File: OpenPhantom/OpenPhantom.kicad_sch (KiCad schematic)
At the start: 94 parts, among them J1 Barrel_Jack, J2 Video, J3 Audio, Q1 BC548, Q2 BD136, Q3 BC557, Q4 BC548, SW1 POWER, SW2 RESET, U1 UM6116 VRAM, U10 74HC368, U11 74HC368, U2 UM6116 WRAM, U3 74HC04, U4 UA6547_CPU, U5 4013, U6 UA6548_PPU, U7 74HC139, U8 74LS373, U9 LM7805_TO220, Y1 21.453366 MHz

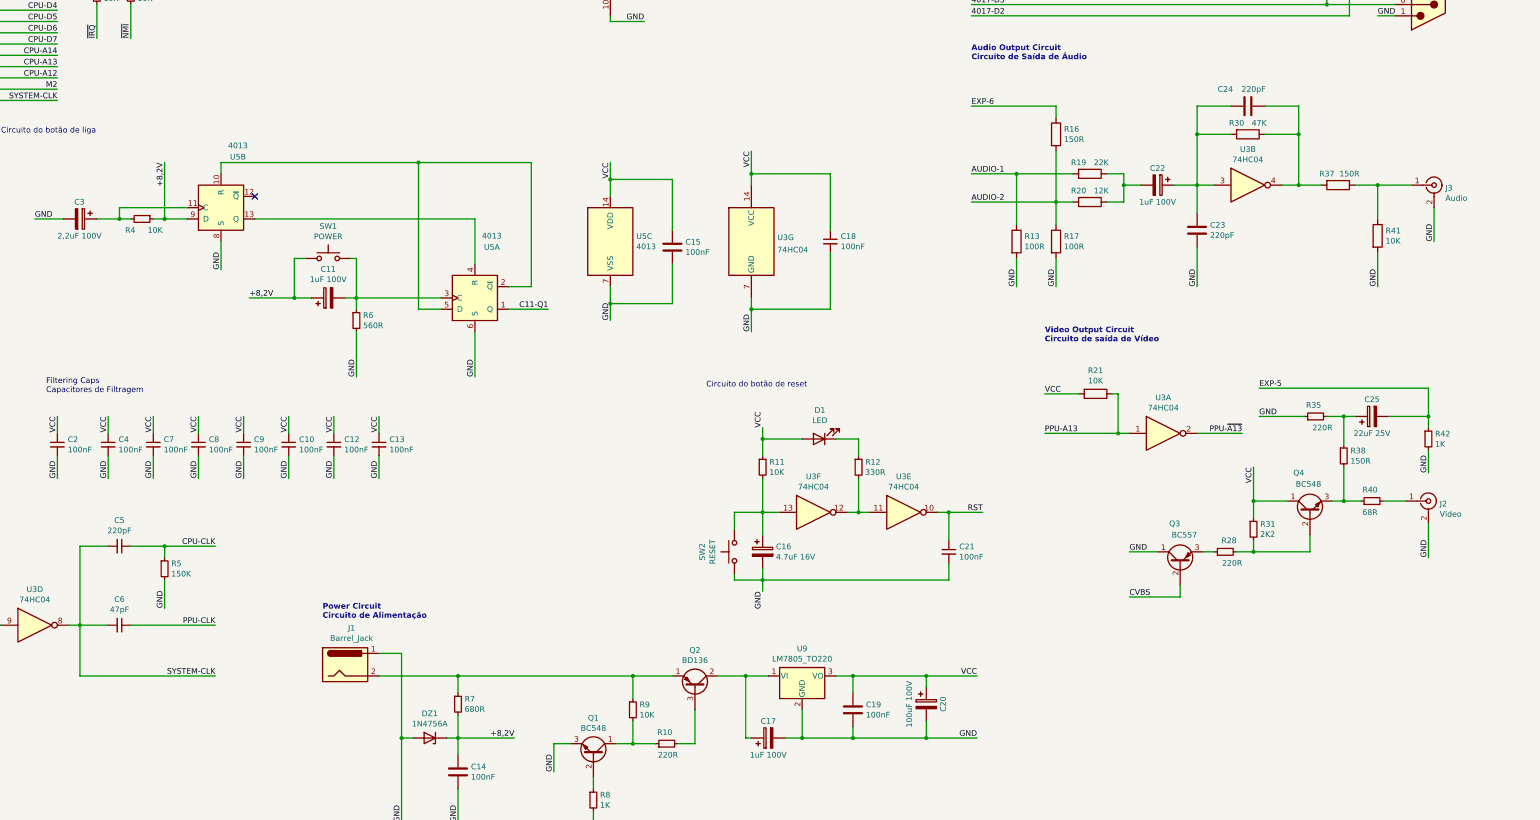
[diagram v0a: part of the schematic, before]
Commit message: PDF + PCB Routing + `Placement
Corrected component position. Added PCB Schematic PDF. Changed the logo. Moved the RCA connectors 2mm closer to the PCB edge.
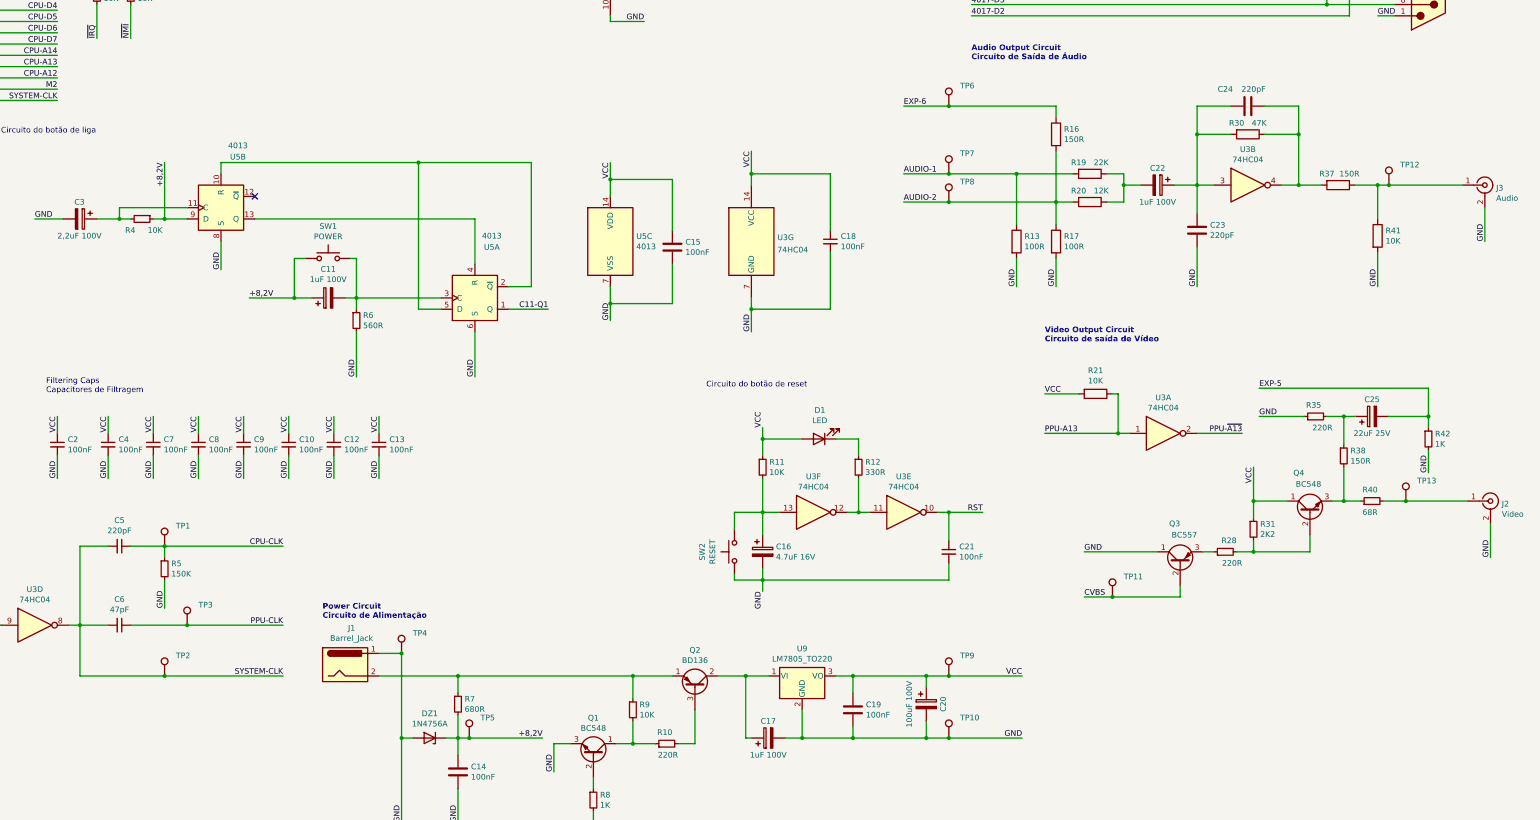
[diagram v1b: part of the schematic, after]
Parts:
- added TP1, TP10, TP11, TP12, TP13, TP2, TP3, TP4, TP5, TP6, TP7, TP8, TP9: (no value), symbol Connector:TestPoint
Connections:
- net +8,2V: now also TP5.1
- net AUDIO-1: now also TP7.1
- net AUDIO-2: now also TP8.1
- net CPU-CLK: now also TP1.1
- net CVBS: now also TP11.1
- net EXP-6: now also TP6.1
- net GND: now also TP10.1, TP4.1
- net PPU-CLK: now also TP3.1
- net SYSTEM-CLK: now also TP2.1
- net VCC: now also TP9.1
- net at J2.1 (In), R40.2: now also TP13.1
- net at J3.1 (In), R37.1, R41.1: now also TP12.1
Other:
- moved on the sheet: J2, J3

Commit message: New BOM + Schematic
Updated Bill of Materials and Schematics
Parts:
- TP1: value (none) -> CPU CLK; footprint (none) -> TestPoint:TestPoint_Pad_1.0x1.0mm
- TP10: value (none) -> GND; footprint (none) -> TestPoint:TestPoint_Pad_1.0x1.0mm
- TP11: value (none) -> PPU CVBS; footprint (none) -> TestPoint:TestPoint_Pad_1.0x1.0mm
- TP12: value (none) -> AUDIO OUT; footprint (none) -> TestPoint:TestPoint_Pad_1.0x1.0mm
- TP13: value (none) -> VIDEO OUT; footprint (none) -> TestPoint:TestPoint_Pad_1.0x1.0mm
- TP2: value (none) -> SYS CLK; footprint (none) -> TestPoint:TestPoint_Pad_1.0x1.0mm
- TP3: value (none) -> PPU CLK; footprint (none) -> TestPoint:TestPoint_Pad_1.0x1.0mm
- TP4: value (none) -> POWER SUPPLY IN; footprint (none) -> TestPoint:TestPoint_Pad_1.0x1.0mm
- TP5: value (none) -> +8,2V; footprint (none) -> TestPoint:TestPoint_Pad_1.0x1.0mm
- TP6: value (none) -> EXP AUDIO; footprint (none) -> TestPoint:TestPoint_Pad_1.0x1.0mm
- TP7: value (none) -> CPU AUDIO 1; footprint (none) -> TestPoint:TestPoint_Pad_1.0x1.0mm
- TP8: value (none) -> CPU AUDIO 2; footprint (none) -> TestPoint:TestPoint_Pad_1.0x1.0mm
- TP9: value (none) -> +5V; footprint (none) -> TestPoint:TestPoint_Pad_1.0x1.0mm
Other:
- note added: "Power button circuit Circuito do botão de liga"
- note added: "Reset button circuit Circuito do botão de reset"
- note removed: "Circuito do botão de liga"
- note removed: "Circuito do botão de reset"
- title: OpenPhantom - Gradiente Phantom System Main Board -> OpenPhantom - Gradiente Phantom System PH-8 Main Board
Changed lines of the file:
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@@
   (paper "A3")
   (title_block
-    (title "OpenPhantom - Gradiente Phantom System Main Board")
+    (title "OpenPhantom - Gradiente Phantom System PH-8 Main Board")
     (date "2022-04-19")
     (rev "4")
+    (comment 1 "Twitter: @vagnerlc")
+    (comment 2 "github.com/vlcampos/OpenPhantom")
+    (comment 3 "Project files at/Arquivos do projeto em:")
   )
   (junction (at 351.79 85.09) (diameter 0) (color 0 0 0 0)
@@
     (effects (font (size 1.27 1.27)) (justify left bottom))
   )
-  (text "Circuito do botão de liga" (at 63.5 119.38 0)
+  (text "Power button circuit\nCircuito do botão de liga" (at 63.5 119.38 0)
     (effects (font (size 1.27 1.27)) (justify left bottom))
   )
@@
     (effects (font (size 1.27 1.27) (thickness 0.254) bold) (justify left bottom))
   )
-  (text "Circuito do botão de reset" (at 222.25 176.53 0)
+  (text "Reset button circuit\nCircuito do botão de reset" (at 222.25 176.53 0)
     (effects (font (size 1.27 1.27)) (justify left bottom))
   )
@@
       (effects (font (size 1.27 1.27)) (justify left))
     )
-    (property "Value" "" (id 1) (at 171.45 253.2379 0)
+    (property "Value" "+8,2V" (id 1) (at 171.45 253.2379 0)
       (effects (font (size 1.27 1.27)) (justify left))
     )
-    (property "Footprint" "" (id 2) (at 173.99 255.27 0)
+    (property "Footprint" "TestPoint:TestPoint_Pad_1.0x1.0mm" (id 2) (at 173.99 255.27 0)
       (effects (font (size 1.27 1.27)) hide)
     )
@@
       (effects (font (size 1.27 1.27)) (justify left))
     )
-    (property "Value" "" (id 1) (at 279.4 126.2379 0)
+    (property "Value" "CPU AUDIO 1" (id 1) (at 279.4 126.2379 0)
       (effects (font (size 1.27 1.27)) (justify left))
     )
-    (property "Footprint" "" (id 2) (at 281.94 128.27 0)
+    (property "Footprint" "TestPoint:TestPoint_Pad_1.0x1.0mm" (id 2) (at 281.94 128.27 0)
       (effects (font (size 1.27 1.27)) hide)
     )
@@
       (effects (font (size 1.27 1.27)) (justify left))
     )
-    (property "Value" "" (id 1) (at 102.87 210.0579 0)
+    (property "Value" "CPU CLK" (id 1) (at 102.87 210.0579 0)
       (effects (font (size 1.27 1.27)) (justify left))
     )
-    (property "Footprint" "" (id 2) (at 105.41 212.09 0)
+    (property "Footprint" "TestPoint:TestPoint_Pad_1.0x1.0mm" (id 2) (at 105.41 212.09 0)
       (effects (font (size 1.27 1.27)) hide)
     )
@@
       (effects (font (size 1.27 1.27)) (justify left))
     )
-    (property "Value" "" (id 1) (at 102.87 239.2679 0)
+    (property "Value" "SYS CLK" (id 1) (at 102.87 239.2679 0)
       (effects (font (size 1.27 1.27)) (justify left))
     )
-    (property "Footprint" "" (id 2) (at 105.41 241.3 0)
+    (property "Footprint" "TestPoint:TestPoint_Pad_1.0x1.0mm" (id 2) (at 105.41 241.3 0)
       (effects (font (size 1.27 1.27)) hide)
     )
@@
       (effects (font (size 1.27 1.27)) (justify left))
     )
-    (property "Value" "" (id 1) (at 107.95 227.8379 0)
+    (property "Value" "PPU CLK" (id 1) (at 107.95 227.8379 0)
       (effects (font (size 1.27 1.27)) (justify left))
     )
-    (property "Footprint" "" (id 2) (at 110.49 229.87 0)
+    (property "Footprint" "TestPoint:TestPoint_Pad_1.0x1.0mm" (id 2) (at 110.49 229.87 0)
       (effects (font (size 1.27 1.27)) hide)
     )
@@
       (effects (font (size 1.27 1.27)) (justify left))
     )
-    (property "Value" "" (id 1) (at 156.21 234.1879 0)
+    (property "Value" "POWER SUPPLY IN" (id 1) (at 156.21 234.1879 0)
       (effects (font (size 1.27 1.27)) (justify left))
     )
-    (property "Footprint" "" (id 2) (at 158.75 236.22 0)
+    (property "Footprint" "TestPoint:TestPoint_Pad_1.0x1.0mm" (id 2) (at 158.75 236.22 0)
       (effects (font (size 1.27 1.27)) hide)
     )
@@
       (effects (font (size 1.27 1.27)) (justify left))
     )
-    (property "Value" "" (id 1) (at 316.23 221.4879 0)
+    (property "Value" "PPU CVBS" (id 1) (at 316.23 221.4879 0)
       (effects (font (size 1.27 1.27)) (justify left))
     )
-    (property "Footprint" "" (id 2) (at 318.77 223.52 0)
+    (property "Footprint" "TestPoint:TestPoint_Pad_1.0x1.0mm" (id 2) (at 318.77 223.52 0)
       (effects (font (size 1.27 1.27)) hide)
     )
@@
       (effects (font (size 1.27 1.27)) (justify left))
     )
-    (property "Value" "" (id 1) (at 279.4 110.9979 0)
+    (property "Value" "EXP AUDIO" (id 1) (at 279.4 110.9979 0)
       (effects (font (size 1.27 1.27)) (justify left))
     )
-    (property "Footprint" "" (id 2) (at 281.94 113.03 0)
+    (property "Footprint" "TestPoint:TestPoint_Pad_1.0x1.0mm" (id 2) (at 281.94 113.03 0)
       (effects (font (size 1.27 1.27)) hide)
     )
@@
       (effects (font (size 1.27 1.27)) (justify left))
     )
-    (property "Value" "" (id 1) (at 382.27 199.8979 0)
+    (property "Value" "VIDEO OUT" (id 1) (at 382.27 199.8979 0)
       (effects (font (size 1.27 1.27)) (justify left))
     )
-    (property "Footprint" "" (id 2) (at 384.81 201.93 0)
+    (property "Footprint" "TestPoint:TestPoint_Pad_1.0x1.0mm" (id 2) (at 384.81 201.93 0)
       (effects (font (size 1.27 1.27)) hide)
     )
@@
       (effects (font (size 1.27 1.27)) (justify left))
     )
-    (property "Value" "" (id 1) (at 378.46 128.7779 0)
+    (property "Value" "AUDIO OUT" (id 1) (at 378.46 128.7779 0)
       (effects (font (size 1.27 1.27)) (justify left))
     )
-    (property "Footprint" "" (id 2) (at 381 130.81 0)
+    (property "Footprint" "TestPoint:TestPoint_Pad_1.0x1.0mm" (id 2) (at 381 130.81 0)
       (effects (font (size 1.27 1.27)) hide)
     )
@@
       (effects (font (size 1.27 1.27)) (justify left))
     )
-    (property "Value" "" (id 1) (at 279.4 239.2679 0)
+    (property "Value" "+5V" (id 1) (at 279.4 239.2679 0)
       (effects (font (size 1.27 1.27)) (justify left))
     )
-    (property "Footprint" "" (id 2) (at 281.94 241.3 0)
+    (property "Footprint" "TestPoint:TestPoint_Pad_1.0x1.0mm" (id 2) (at 281.94 241.3 0)
       (effects (font (size 1.27 1.27)) hide)
     )
@@
       (effects (font (size 1.27 1.27)) (justify left))
     )
-    (property "Value" "" (id 1) (at 279.4 253.2379 0)
+    (property "Value" "GND" (id 1) (at 279.4 253.2379 0)
       (effects (font (size 1.27 1.27)) (justify left))
     )
-    (property "Footprint" "" (id 2) (at 281.94 255.27 0)
+    (property "Footprint" "TestPoint:TestPoint_Pad_1.0x1.0mm" (id 2) (at 281.94 255.27 0)
       (effects (font (size 1.27 1.27)) hide)
     )
@@
       (effects (font (size 1.27 1.27)) (justify left))
     )
-    (property "Value" "" (id 1) (at 279.4 132.5879 0)
+    (property "Value" "CPU AUDIO 2" (id 1) (at 279.4 132.5879 0)
       (effects (font (size 1.27 1.27)) (justify left))
     )
-    (property "Footprint" "" (id 2) (at 281.94 134.62 0)
+    (property "Footprint" "TestPoint:TestPoint_Pad_1.0x1.0mm" (id 2) (at 281.94 134.62 0)
       (effects (font (size 1.27 1.27)) hide)
     )

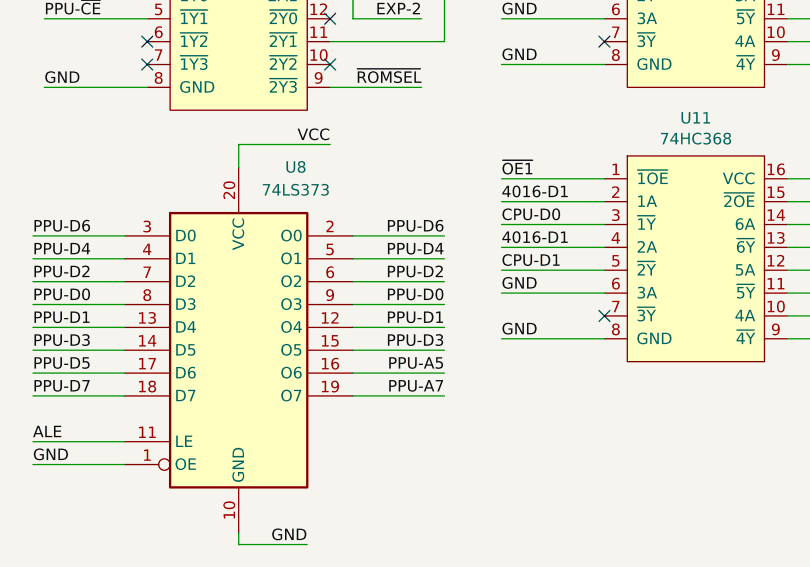
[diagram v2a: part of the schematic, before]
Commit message: 74LS373 PPU AD Pins FIX
Fixed 74LS373 pins connected to the AD Pins from PPU (PPU D0 to D7)
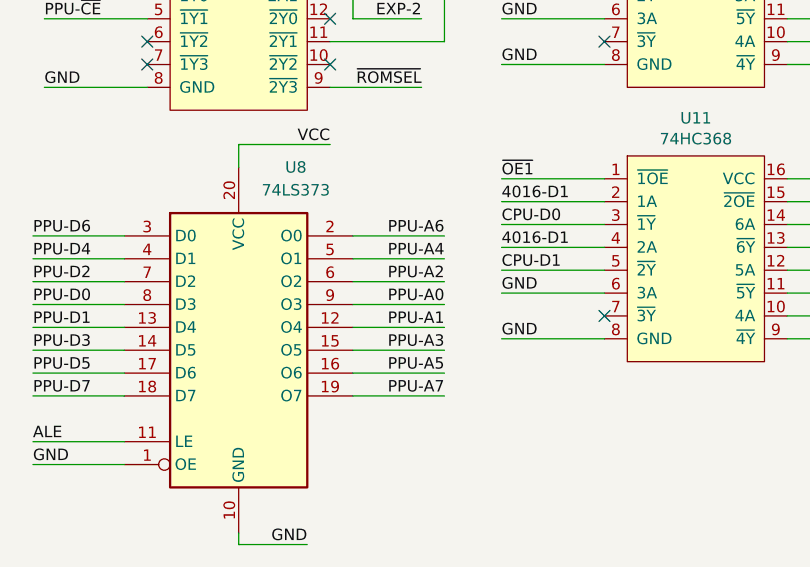
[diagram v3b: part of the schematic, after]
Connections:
- net PPU-A0: now also U8.9 (O3)
- net PPU-A1: now also U8.12 (O4)
- net PPU-A2: now also U8.6 (O2)
- net PPU-A3: now also U8.15 (O5)
- net PPU-A4: now also U8.5 (O1)
- net PPU-A6: now also U8.2 (O0)
- net PPU-D0: no longer U8.9 (O3)
- net PPU-D1: no longer U8.12 (O4)
- net PPU-D2: no longer U8.6 (O2)
- net PPU-D3: no longer U8.15 (O5)
- net PPU-D4: no longer U8.5 (O1)
- net PPU-D6: no longer U8.2 (O0)
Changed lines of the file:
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@@
   (title_block
     (title "OpenPhantom - Gradiente Phantom System PH-8 Main Board")
-    (date "2022-04-19")
-    (rev "4")
+    (date "2022-06-22")
+    (rev "5")
     (comment 1 "Twitter: @vagnerlc")
     (comment 2 "github.com/vlcampos/OpenPhantom")
@@
     (effects (font (size 1.27 1.27)) (justify right bottom))
   )
-  (label "PPU-D3" (at 223.52 72.39 180)
+  (label "PPU-A3" (at 223.52 72.39 180)
     (effects (font (size 1.27 1.27)) (justify right bottom))
   )
@@
     (effects (font (size 1.27 1.27)) (justify right bottom))
   )
-  (label "PPU-D1" (at 223.52 69.85 180)
+  (label "PPU-A1" (at 223.52 69.85 180)
     (effects (font (size 1.27 1.27)) (justify right bottom))
   )
@@
     (effects (font (size 1.27 1.27)) (justify right bottom))
   )
-  (label "PPU-D0" (at 223.52 67.31 180)
+  (label "PPU-A0" (at 223.52 67.31 180)
     (effects (font (size 1.27 1.27)) (justify right bottom))
   )
@@
     (effects (font (size 1.27 1.27)) (justify left bottom))
   )
-  (label "PPU-D6" (at 223.52 59.69 180)
+  (label "PPU-A6" (at 223.52 59.69 180)
     (effects (font (size 1.27 1.27)) (justify right bottom))
   )
@@
     (effects (font (size 1.27 1.27)) (justify left bottom))
   )
-  (label "PPU-D2" (at 223.52 64.77 180)
+  (label "PPU-A2" (at 223.52 64.77 180)
     (effects (font (size 1.27 1.27)) (justify right bottom))
   )
@@
     (effects (font (size 1.27 1.27)) (justify right bottom))
   )
-  (label "PPU-D4" (at 223.52 62.23 180)
-    (effects (font (size 1.27 1.27)) (justify right bottom))
-  )
+  (label "PPU-A4" (at 223.52 62.23 180)
+    (effects (font (size 1.27 1.27)) (justify right bottom))
+  )

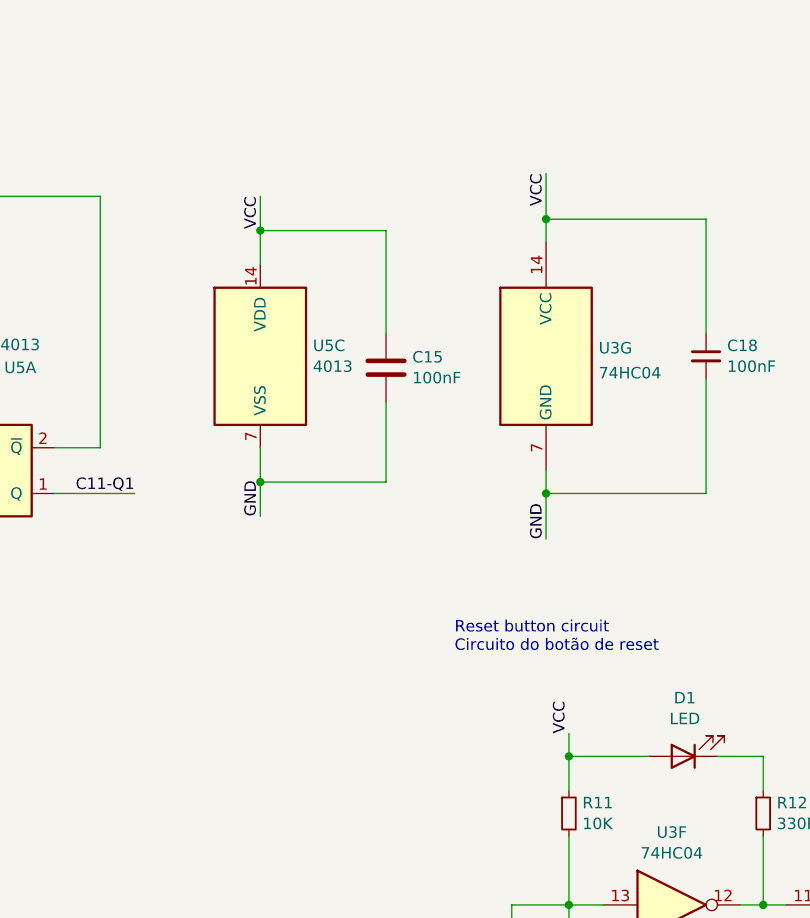
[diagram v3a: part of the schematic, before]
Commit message: Fixed Routes
Power route fix.
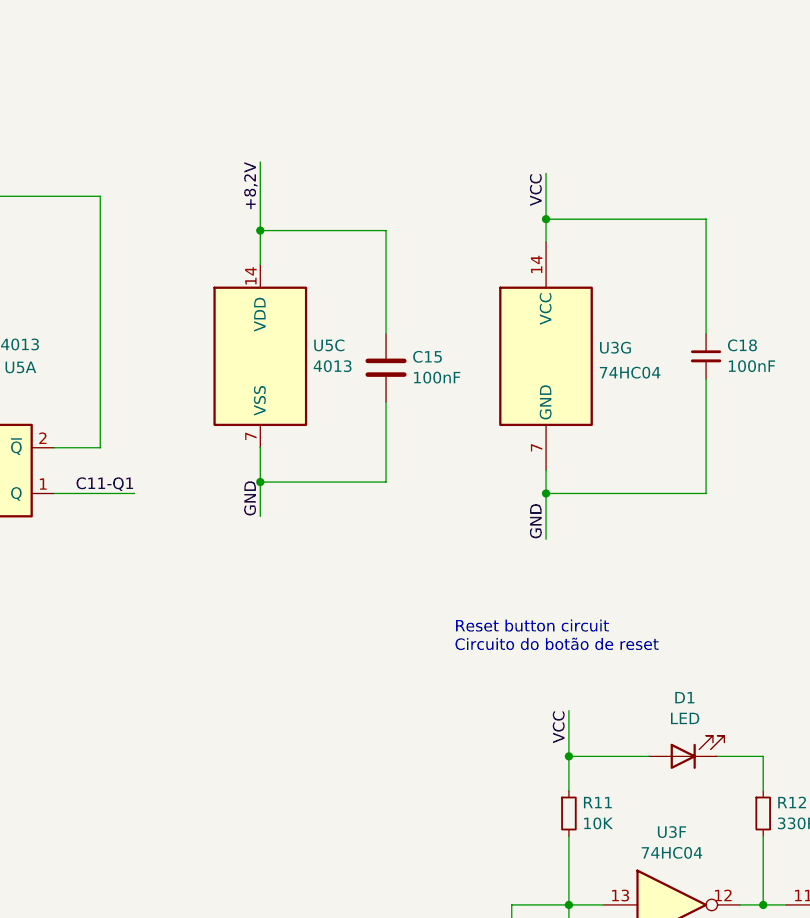
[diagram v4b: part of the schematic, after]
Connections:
- net +8,2V: now also C15.1, U5.14 (VDD)
- net VCC: no longer C15.1, U5.14 (VDD)
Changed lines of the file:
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@@
     (stroke (width 0) (type default) (color 0 0 0 0))
   )
-  (wire (pts (xy 200.66 129.54) (xy 200.66 125.73))
+  (wire (pts (xy 200.66 129.54) (xy 200.66 121.92))
     (stroke (width 0) (type default) (color 0 0 0 0))
   )
@@
     (stroke (width 0) (type default) (color 0 0 0 0))
   )
-  (wire (pts (xy 234.95 185.42) (xy 234.95 187.96))
+  (wire (pts (xy 234.95 182.88) (xy 234.95 187.96))
     (stroke (width 0) (type default) (color 0 0 0 0))
   )
@@
     (effects (font (size 1.27 1.27)) (justify right bottom))
   )
-  (label "VCC" (at 200.66 125.73 270)
+  (label "+8,2V" (at 200.66 121.92 270)
     (effects (font (size 1.27 1.27)) (justify right bottom))
   )
@@
     (effects (font (size 1.27 1.27)) (justify right bottom))
   )
-  (label "VCC" (at 234.95 185.42 90)
-    (effects (font (size 1.27 1.27)) (justify left bottom))
+  (label "VCC" (at 234.95 182.88 270)
+    (effects (font (size 1.27 1.27)) (justify right bottom))
   )
   (label "~{ROMSEL}" (at 76.2 78.74 180)
